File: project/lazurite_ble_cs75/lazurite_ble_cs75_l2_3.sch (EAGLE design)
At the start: 11 parts

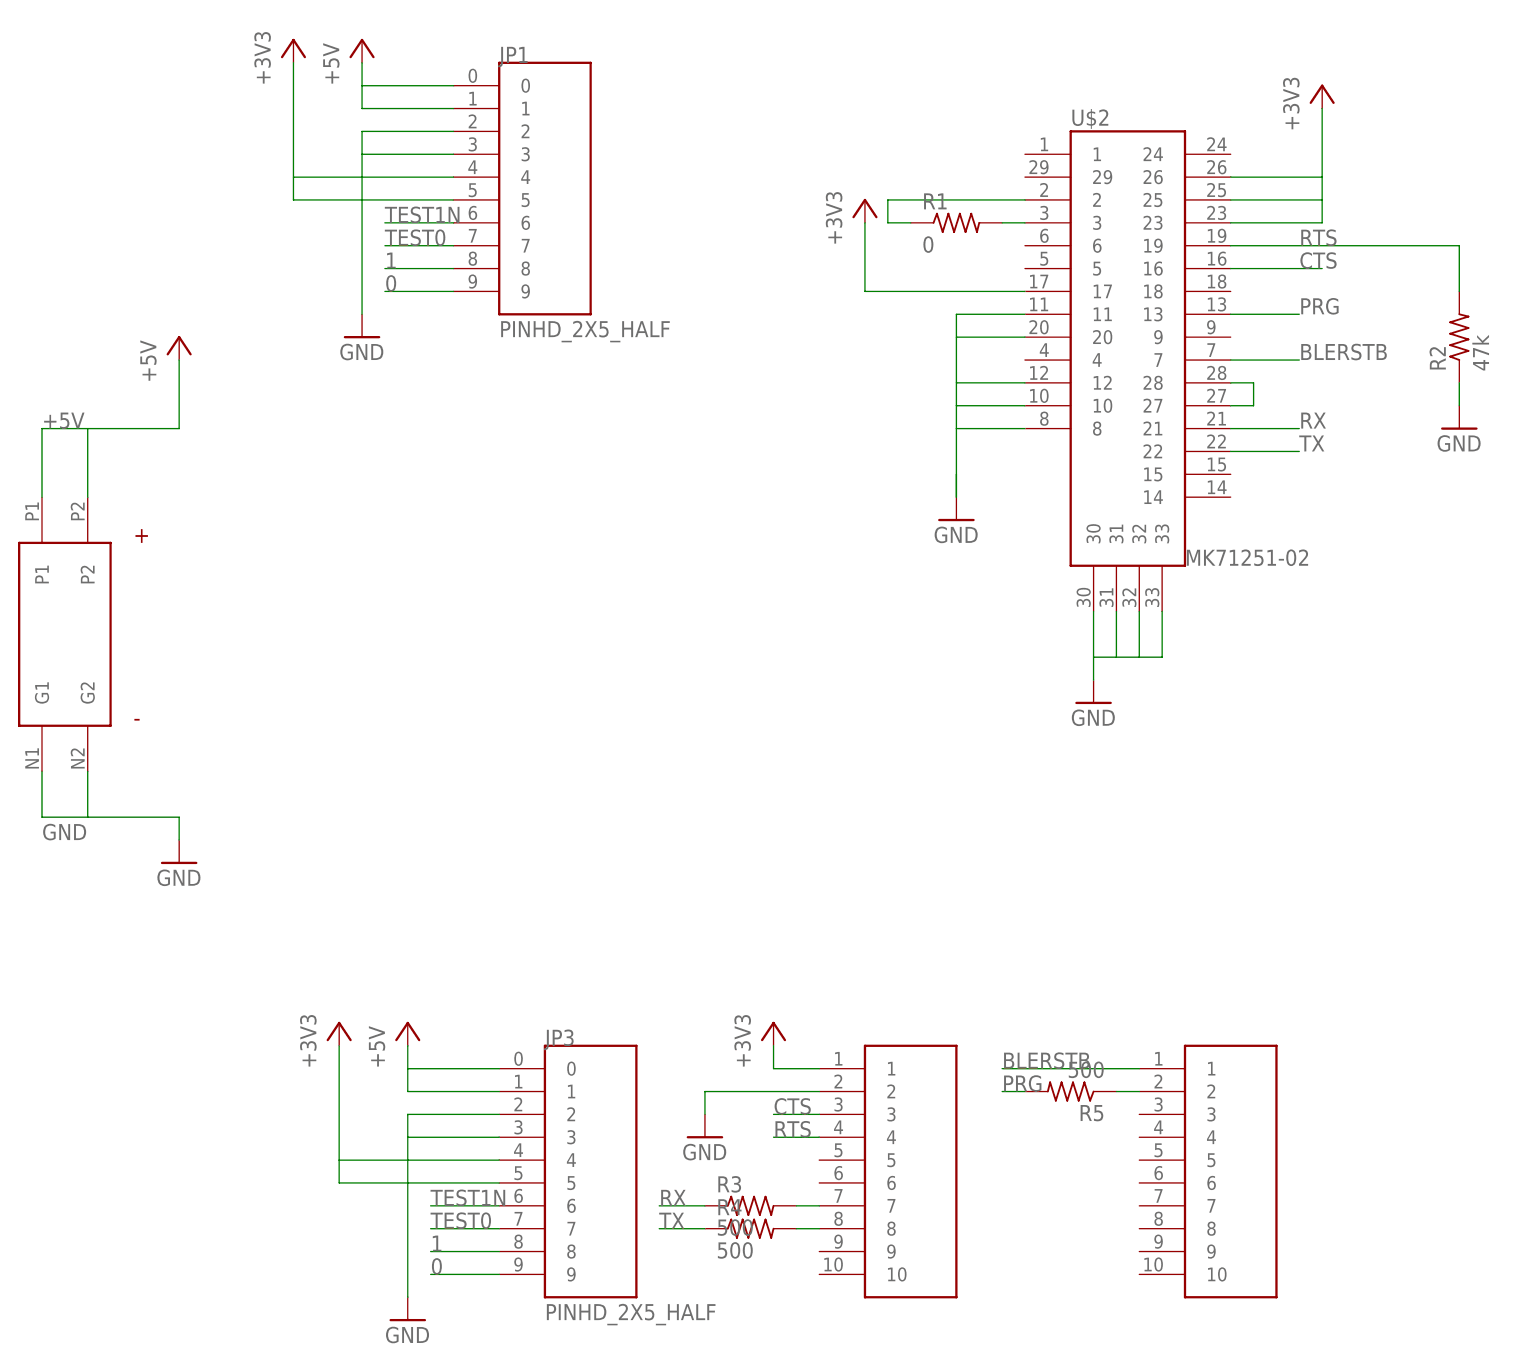
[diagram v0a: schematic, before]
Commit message: update libraries and all schematic/board data.
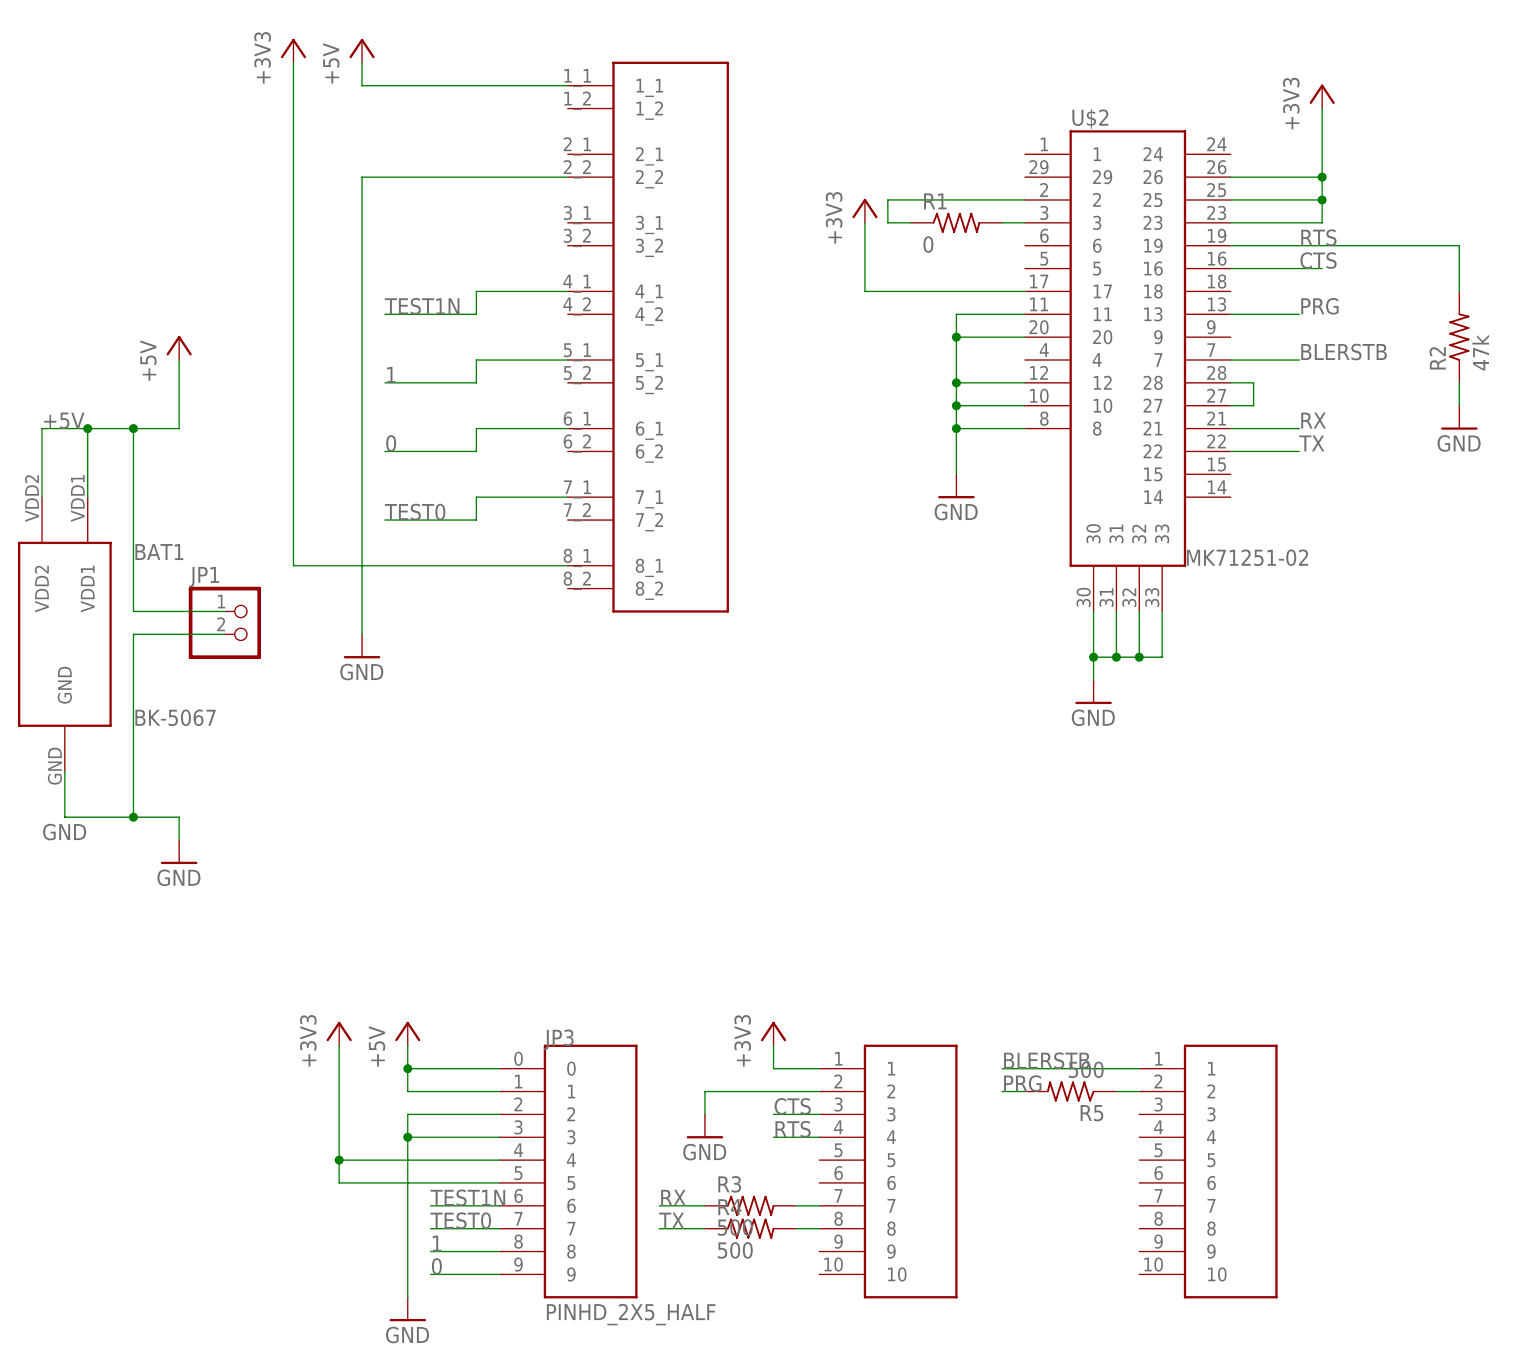
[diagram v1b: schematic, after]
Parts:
- added BAT1: BK-5067, lz-shield:BK-5067
- JP1: value PINHD_2X5_HALF -> (none); device lazurite:PINHD_2X5_HALF -> pinhead:PINHD-1X2
- U$1: value TAKACHI_CS75_BATTERY -> XB-1-X; device lz-shield:TAKACHI_CS75_BATTERY -> lz-shield:XB-1-X
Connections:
- net +3V3: now also U$1.8_1; no longer JP1.4, JP1.5
- net +5V: now also BAT1.VDD1, BAT1.VDD2, U$1.1_1; no longer JP1.0, U$1.P1, U$1.P2
- net 0: now also U$1.6_1; no longer JP1.9
- net 1: now also U$1.5_1; no longer JP1.8
- net GND: now also BAT1.GND, U$1.2_2; no longer JP1.3, U$1.G1, U$1.G2
- net TEST0: now also U$1.7_1; no longer JP1.7
- net TEST1N: now also U$1.4_1; no longer JP1.6
